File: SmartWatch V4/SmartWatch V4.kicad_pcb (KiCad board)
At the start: 4 copper layers, 46.8 x 34.8 mm, 66 parts, among them J1 10118192-0001LF, J10 TestPad, J11 TestPad, J12 TestPad, J13 TestPad, J14 TestPad, J2 , J3 TestPad, J4 TestPad, J5 TestPad, J6 TestPad, J7 TestPad, J8 TestPad, J9 TestPad, Q1 FDN340P, Q2 MMBT3904, Q3 MMBT3904, Q4 FDN340P, SW1 EVQ-P7J01P, SW2 EVQ-P7J01P, U1 MAX17260, U10 TSC2003IPWR, U11 NHD-1.8-128160EF-CTXI#-T, U2 FT231XQ, U3 LP5912-3.3DRVT, U4 LP5912-2.8DRVT, U5 MCP73832-2-OT, U6 ESP32-WROOM-32, U7 NLSV4T244, U8 NLSV4T244, U9 NLSV4T244

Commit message: Edits to Rev 4 board
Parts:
- removed R22: 100k, Resistor_SMD:R_0603_1608Metric
- removed U11: NHD-1.8-128160EF-CTXI#-T, CustomFootprints:LCD_NHD-1.8-128160EF-CTXI#-T
- removed U7, U8, U9: NLSV4T244, CustomFootprints:NLSV4T244MUTAG
- added A1: NHD-1.8-128160EF-CTXI#-T, CustomFootprints:ZJY117, B.Cu at (127.2, 79.6)
- added J15: TestPad, CustomFootprints:TESTPAD, B.Cu at (152.2, 76.2)
- added J16: TestPad, CustomFootprints:TESTPAD, B.Cu at (150.6, 78.2)
- added J17: TestPad, CustomFootprints:TESTPAD, B.Cu at (153.4, 78.2)
- added J18: TestPad, CustomFootprints:TESTPAD, B.Cu at (150.6, 66.4)
- added J19: TestPad, CustomFootprints:TESTPAD, B.Cu at (149.4, 69.0)
- added J20: TestPad, CustomFootprints:TESTPAD, B.Cu at (148.2, 67.2)
- Q4: value FDN340P -> 2N7002K
- R20: value 100k -> 0 (NC)
- U4: value LP5912-2.8DRVT -> LP5912-3.3DRVT
- moved J6 7.25 mm to (141.3, 76.1)
- moved R20 4.10 mm to (138.3, 75.7), turned to 0 degrees
- moved Q4 2.29 mm to (138.4, 78.4), turned to 270 degrees
- moved U4 0.35 mm to (144.4, 92.0)
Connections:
- C6 pad 1: +2V8 -> /LCD_PWR
- C9 pad 1: +2V8 -> /LCD_PWR
- J1 pad 4: Net-(J1-Pad4) -> (no net)
- Q4 pad 2: /LED_PWR -> GND
- Q4 pad 3: +3V3 -> /LCD_CATHODE
- R20 pad 1: +2V8 -> GND
- R20 pad 2: /LCD_~RST~ -> /LCD_CATHODE
- R4 pad 2: +3V3 -> /BAT+
- U10 pad 15: Net-(U10-Pad15) -> (no net)
- U10 pad 16: Net-(U10-Pad16) -> (no net)
- U10 pad 7: Net-(U10-Pad7) -> (no net)
- U10 pad 8: Net-(U10-Pad8) -> (no net)
- U2 pad 2: Net-(U2-Pad2) -> (no net)
- U2 pad 4: Net-(U2-Pad4) -> (no net)
- U2 pad 5: Net-(U2-Pad5) -> (no net)
- U2 pad 6: Net-(U2-Pad6) -> (no net)
- U4 pad 1: +2V8 -> /LCD_PWR
- U4 pad 4: /IO12 -> /LCD_EN
- U6 pad 10: /LCD_DB2 -> Net-(J18-Pad1)
- U6 pad 11: /LCD_DB1 -> Net-(J19-Pad1)
- U6 pad 12: /LCD_DB0 -> Net-(J20-Pad1)
- U6 pad 13: /LCD_DB5 -> /LCD_CS
- U6 pad 16: /LCD_~RST~ -> /LCD_EN
- U6 pad 17: Net-(U6-Pad17) -> (no net)
- U6 pad 18: Net-(U6-Pad18) -> (no net)
- U6 pad 19: Net-(U6-Pad19) -> (no net)
- U6 pad 20: Net-(U6-Pad20) -> (no net)
- U6 pad 21: Net-(U6-Pad21) -> (no net)
- U6 pad 22: Net-(U6-Pad22) -> (no net)
- U6 pad 28: /LCD_~RD~ -> Net-(J16-Pad1)
- U6 pad 29: /LCD_~CS~ -> Net-(J15-Pad1)
- U6 pad 30: /LCD_~DC~ -> /LCD_SCK
- U6 pad 31: /LCD_DB7 -> Net-(J17-Pad1)
- U6 pad 32: Net-(U6-Pad32) -> (no net)
- U6 pad 33: /LCD_DB6 -> /LCD_A0
- U6 pad 36: /I2C_SCL -> /LCD_RST
- U6 pad 37: /I2C_SDA -> /LCD_MOSI
- U6 pad 8: /LCD_DB4 -> /I2C_SCL
- U6 pad 9: /LCD_DB3 -> /I2C_SDA
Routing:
- net /LCD_MOSI: track 0.00 -> 45.0 mm, vias 0 -> 1
- net /LCD_EN: track 0.00 -> 44.2 mm, vias 0 -> 4
- net /LCD_RST: track 0.00 -> 41.9 mm, vias 0 -> 1
- net /LCD_A0: track 0.00 -> 37.8 mm, vias 0 -> 1
- net /LCD_SCK: track 0.00 -> 35.7 mm, vias 0 -> 1
- net /LCD_PWR: track 0.00 -> 35.4 mm, vias 0 -> 12
- net /IO15: track 32.8 -> 4.33 mm, vias 2 -> 0
- net /LCD_~DC~: track 26.6 -> 0.00 mm, vias 2 -> 0
- net /LCD_CS: track 0.00 -> 26.1 mm, vias 0 -> 1
- net /LCD_DB4: track 26.1 -> 0.00 mm, vias 2 -> 0
- net /LCD_~RD~: track 24.8 -> 0.00 mm, vias 2 -> 0
- net /I2C_SCL: track 13.2 -> 37.9 mm, vias 0 -> 2
- net /LCD_~CS~: track 24.7 -> 0.00 mm, vias 2 -> 0
- net Net-(U11-Pad8): track 23.4 -> 0.00 mm, vias 1 -> 0
- net /I2C_SDA: track 14.0 -> 36.3 mm, vias 2 -> 4
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- added copper zone on F.Cu, net /LCD_PWR
- removed copper zone on B.Cu, net +2V8
- removed copper zone on F.Cu, net +2V8
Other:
- board text added: "ESP32 Smartwatch Rev 4.1 Matthew James Bellafaire"
- board text removed: "ESP32 Smartwatch Rev 4 Matthew James Bellafaire"

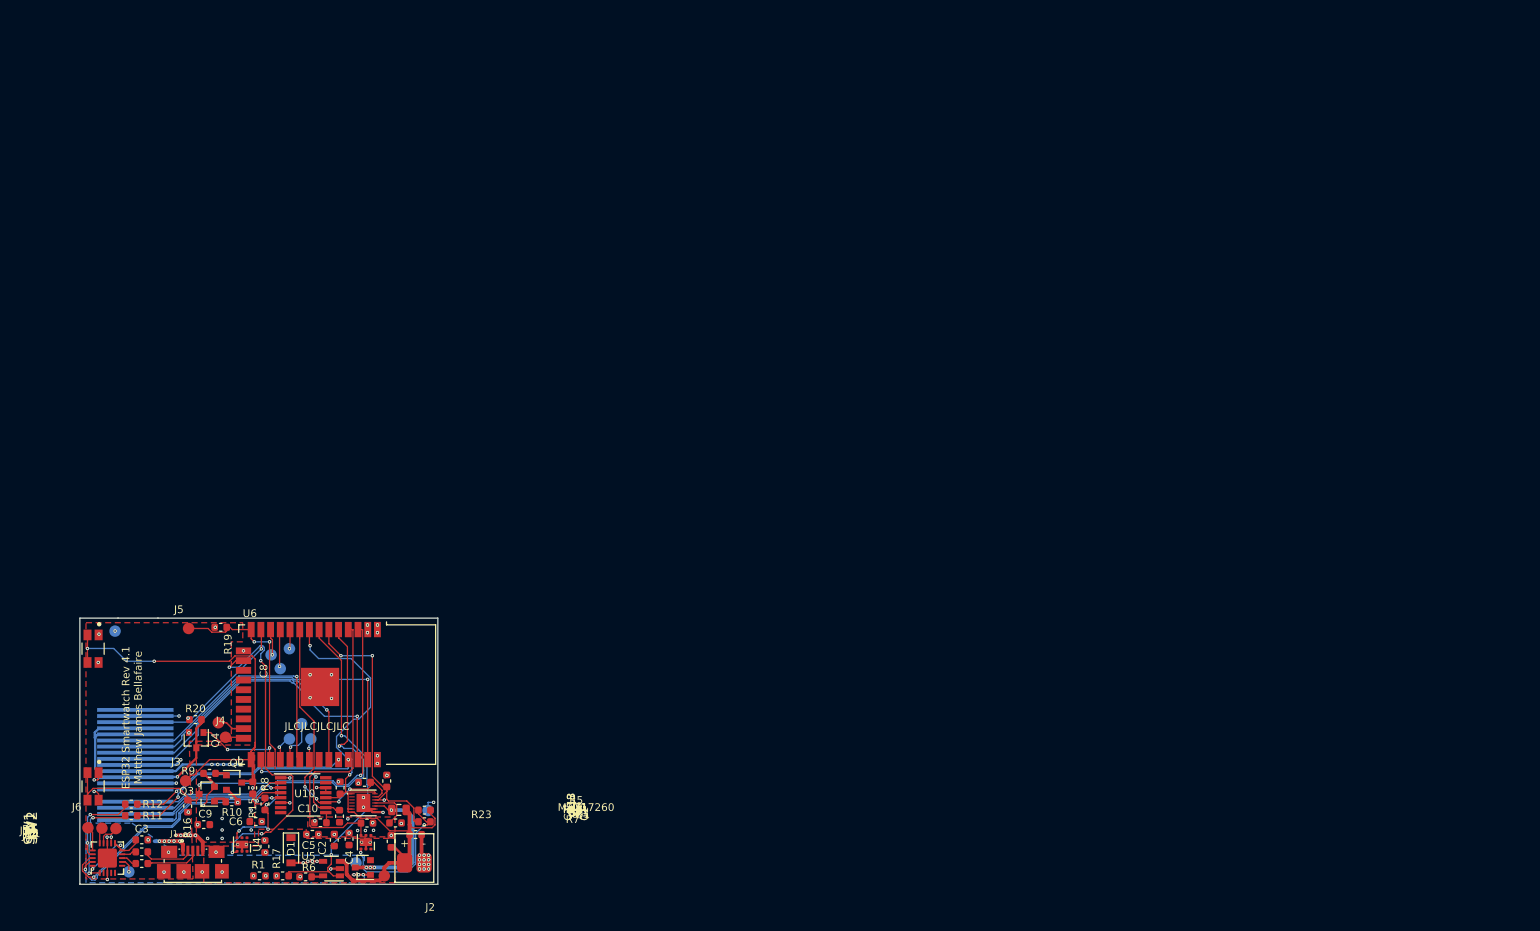
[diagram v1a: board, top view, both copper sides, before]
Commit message: Finished design of Rev 4.1 board and ordered
- Also created an I2C device test program to aid assembly and future code
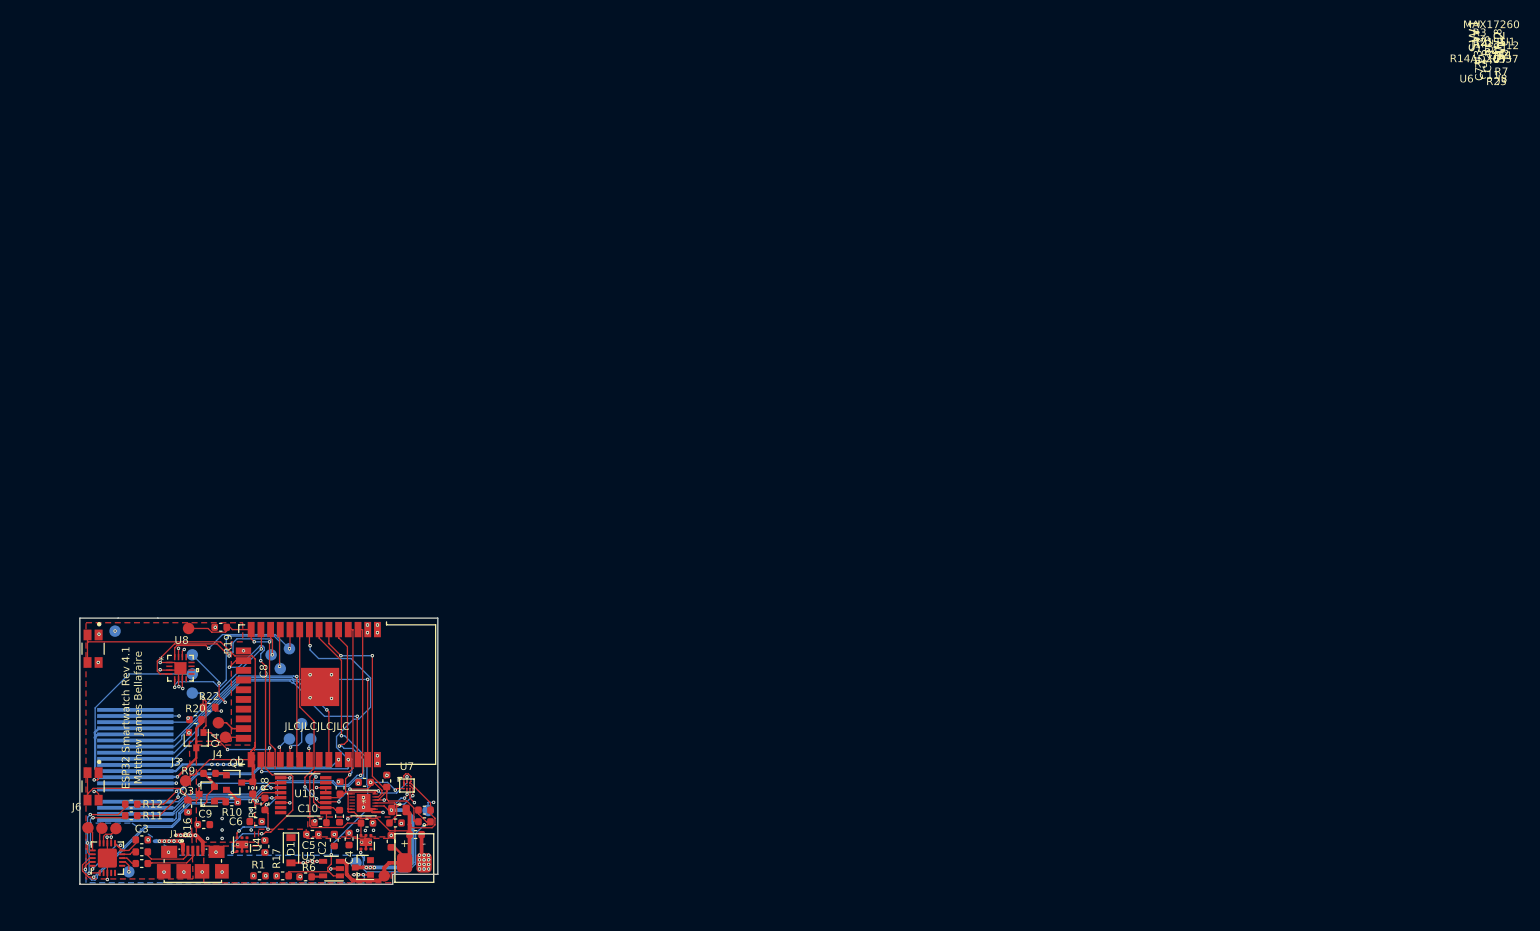
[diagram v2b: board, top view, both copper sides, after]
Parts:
- added J21: TestPad, CustomFootprints:TESTPAD, B.Cu at (137.9, 72.2)
- added J22: TestPad, CustomFootprints:TESTPAD, B.Cu at (137.9, 69.7)
- added J23: TestPad, CustomFootprints:TESTPAD, B.Cu at (137.9, 67.2)
- added R22: 10k, Resistor_SMD:R_0603_1608Metric, F.Cu at (140.1, 74.0)
- added U7: MAX17260_WLP, CustomFootprints:Maxim_WLP-9_1.595x1.415_Layout3x3_P0.4mm_Ball0.27mm_Pad0.25mm_NSMD, F.Cu at (166.0, 84.3)
- added U8: ADXL337, CustomFootprints:ADXL337BCPZ-RL, F.Cu at (136.3, 69.0)
- A1: value NHD-1.8-128160EF-CTXI#-T -> ZJY117
- R23: value 6m -> 10m
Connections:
- net Net-(C11-Pad1) renamed /MAX_REG
- net Net-(J18-Pad1) renamed /Z_ACCEL
- net Net-(J19-Pad1) renamed /X_ACCEL
- net Net-(J20-Pad1) renamed /Y_ACCEL
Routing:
- net /X_ACCEL: track 5.18 -> 30.1 mm, vias 1 -> 2
- net /Y_ACCEL: track 3.40 -> 26.7 mm, vias 1 -> 2
- net /LCD_PWR: track 35.4 -> 53.6 mm
- net /Z_ACCEL: track 2.53 -> 20.5 mm, vias 1 -> 2
- net GND: track 49.5 -> 63.6 mm, vias 63 -> 69
- net /LCD_RST: track 41.9 -> 50.5 mm, vias 1 -> 3
- net /BAT+: track 41.2 -> 49.7 mm
- net /LCD_LED: track 11.4 -> 19.2 mm, vias 2 -> 3
- net /I2C_SCL: track 37.9 -> 44.6 mm, vias 2 -> 4
- net /I2C_SDA: track 36.3 -> 41.2 mm, vias 4 -> 6
- net /MAX_REG: track 5.70 -> 10.1 mm, vias 0 -> 2
- net /BAT_SENSE: track 20.3 -> 24.3 mm, vias 4 -> 6
- net +3V3: track 8.07 -> 10.3 mm, vias 18 -> 20
- net /IO0: track 57.1 -> 57.0 mm, vias 2 -> 0
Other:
- outline, holes or cut-outs redrawn
